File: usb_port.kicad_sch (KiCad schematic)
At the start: 14 parts, among them J1 USB_C_Receptacle, U14 MT9700

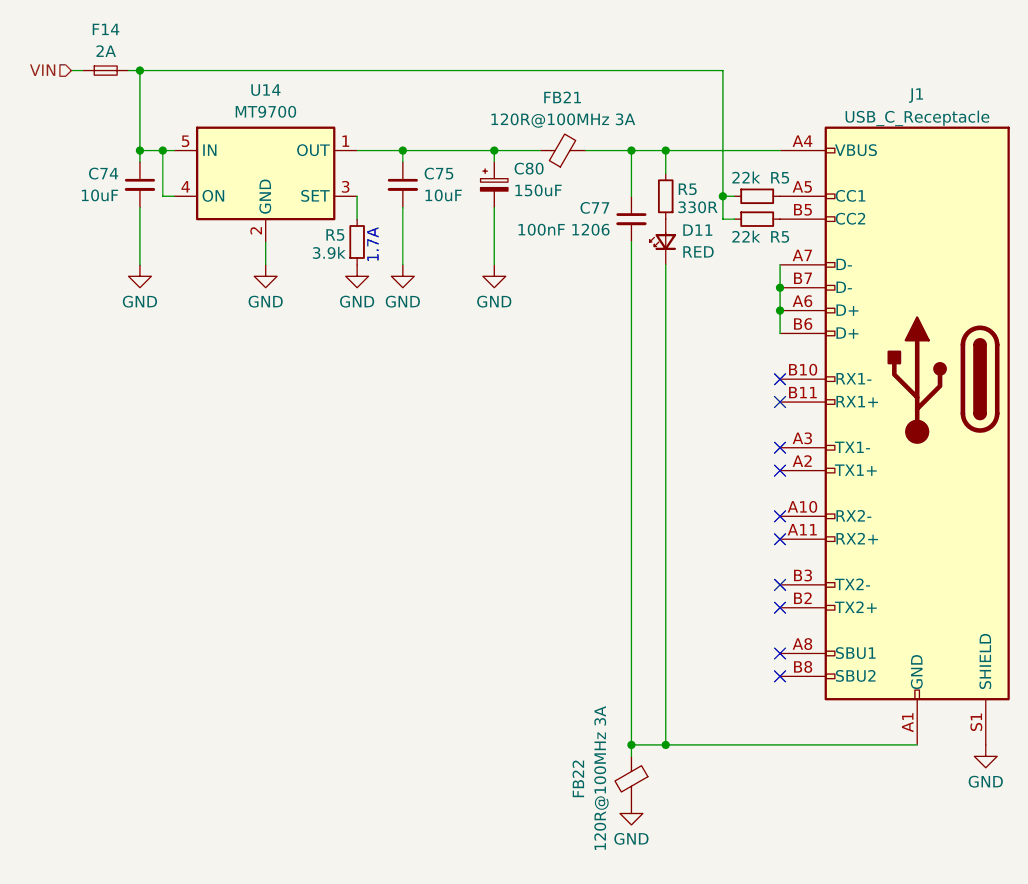
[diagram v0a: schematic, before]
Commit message: Add 5V auxiliary supply
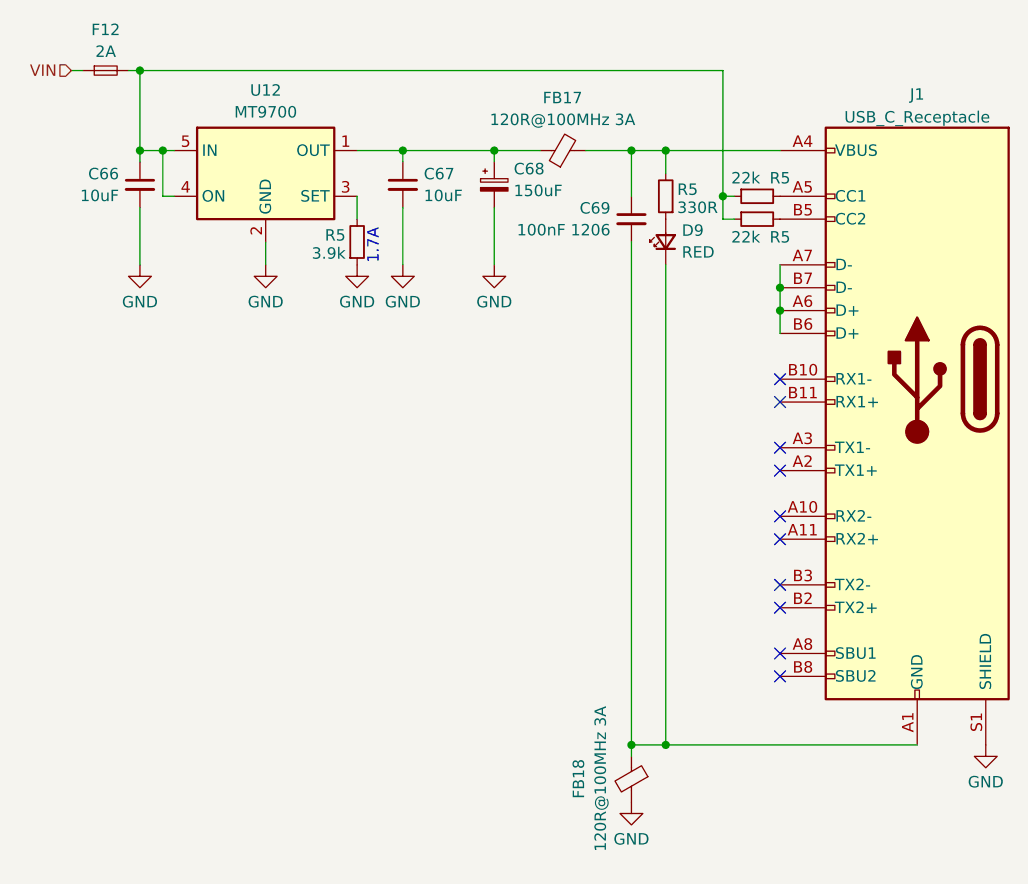
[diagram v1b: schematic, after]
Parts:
- renumbered C74 to C66, C75 to C67, C80 to C68, C77 to C69, D11 to D9, F14 to F12, FB21 to FB17, FB22 to FB18, U14 to U12

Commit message: Reduce LED drive current
The LEDs are very bright when driven with a full 10mA.
Reduce the drive current a bit to make them less intense.
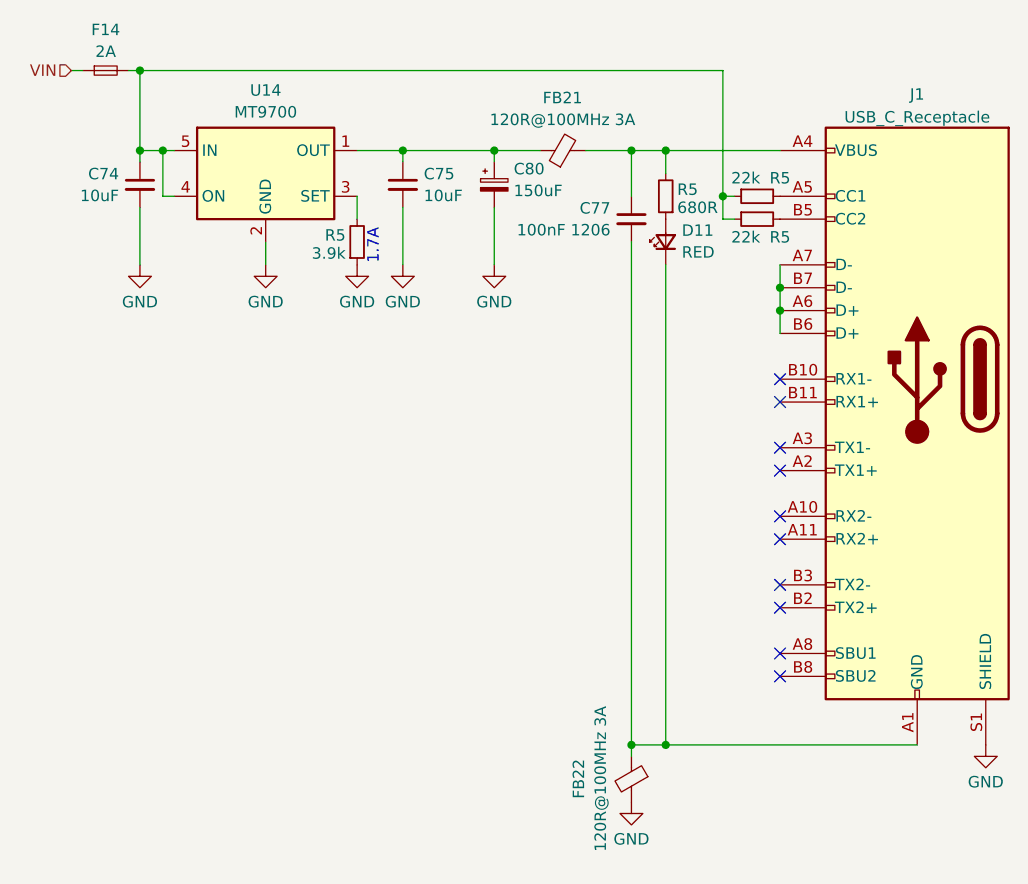
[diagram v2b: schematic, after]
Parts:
- R5: value 330R -> 680R; LCSC C25104 -> C25130
- renumbered C66 to C74, C67 to C75, C69 to C77, C68 to C80, D9 to D11, F12 to F14, FB17 to FB21, FB18 to FB22, U12 to U14
